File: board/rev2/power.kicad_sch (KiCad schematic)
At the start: 16 parts, among them J1 USB_C_Receptacle_USB2.0_14P, J2 Screw_Terminal_01x02, SW4 MS-22D28-G020, U7 TPD6S300A, U8 TPS62933F

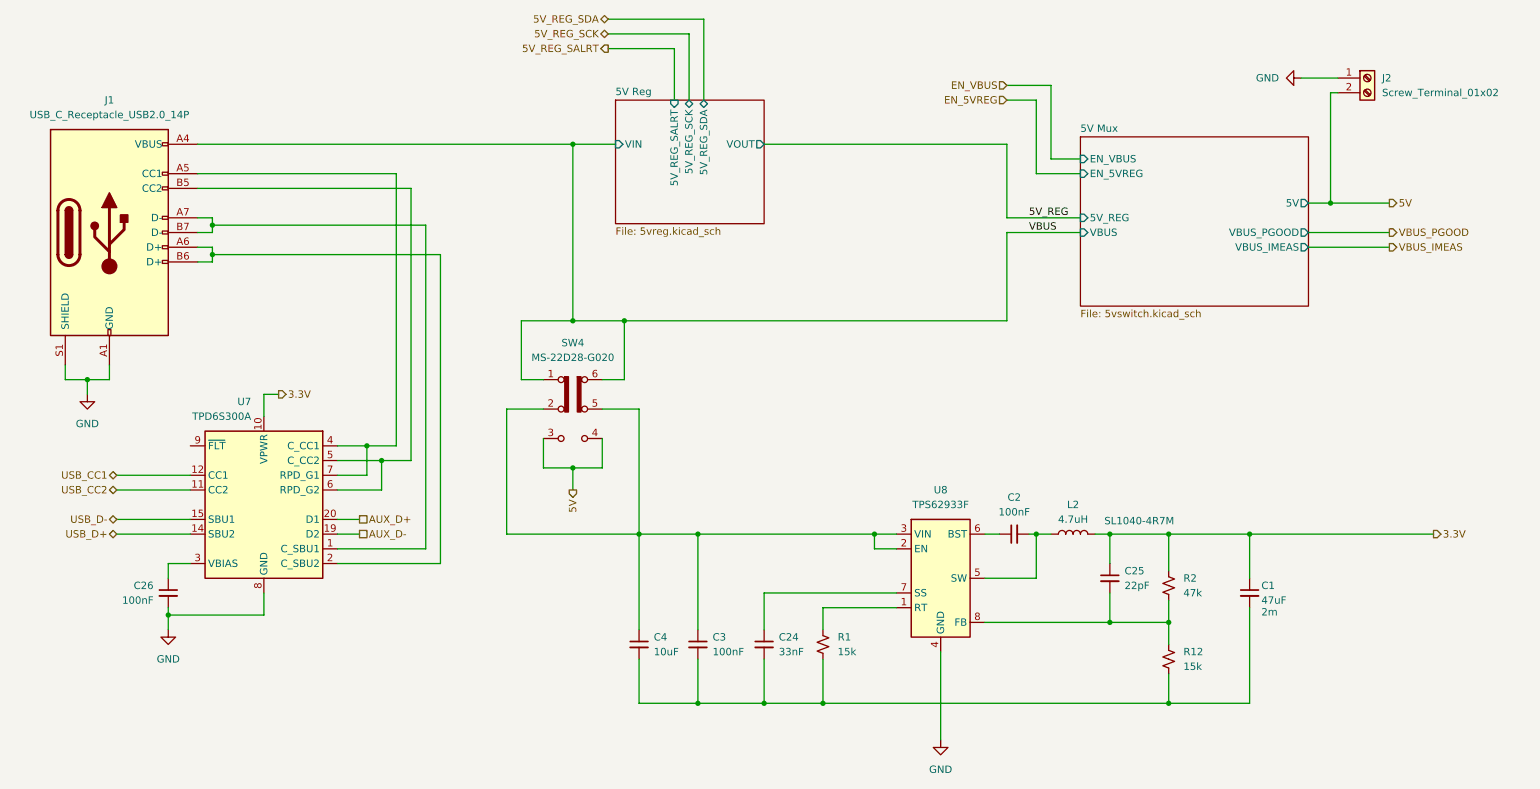
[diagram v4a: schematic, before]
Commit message: Start new PCB
- all footprints setup
- need to setup netclasses next, tho
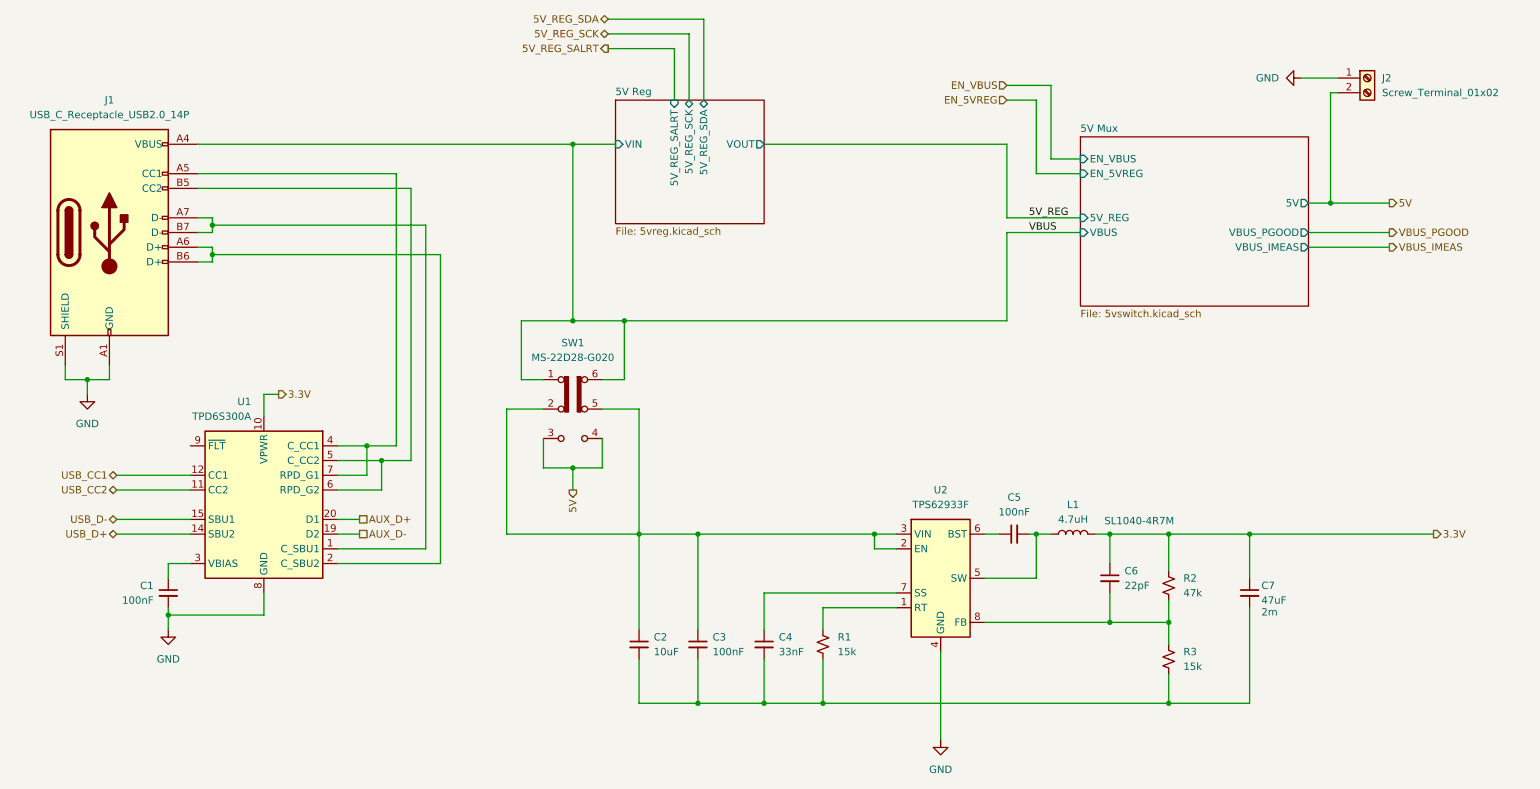
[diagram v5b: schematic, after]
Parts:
- J1: footprint (none) -> Connector_USB:USB_C_Receptacle_HRO_TYPE-C-31-M-12; Part (none) -> TYPE-C-31-M-12
- SW1: renamed from SW4; footprint (none) -> Switch_Slide_SMD:SW-SMD_MS-22D28-G020; Part (none) -> MS-22D28-G020
- U1: renamed from U7; Part (none) -> TPD6S300A
- U2: renamed from U8; Part (none) -> TPS62933F
- renumbered C26 to C1, C4 to C2, C24 to C4, C2 to C5, C25 to C6, C1 to C7, L2 to L1, R12 to R3
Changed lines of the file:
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@@
 		(on_board yes)
 		(dnp no)
-		(property "Reference" "C1"
+		(property "Reference" "C7"
 			(at 238.252 127 0)
 			(effects
@@
 			(project "mainboard"
 				(path "/32eb05c7-b4a6-42f3-8fb3-43453631100f/802d77e5-f72d-443e-abfe-d20b44acef6c"
-					(reference "C1")
+					(reference "C7")
 					(unit 1)
 				)
@@
 		(dnp no)
 		(fields_autoplaced yes)
-		(property "Reference" "#PWR021"
+		(property "Reference" "#PWR04"
 			(at 49.53 140.97 0)
 			(effects
@@
 			(project "mainboard"
 				(path "/32eb05c7-b4a6-42f3-8fb3-43453631100f/802d77e5-f72d-443e-abfe-d20b44acef6c"
-					(reference "#PWR021")
+					(reference "#PWR04")
 					(unit 1)
 				)
@@
 		(dnp no)
 		(fields_autoplaced yes)
-		(property "Reference" "C2"
+		(property "Reference" "C5"
 			(at 195.5863 111.76 90)
 			(effects
@@
 			(project ""
 				(path "/32eb05c7-b4a6-42f3-8fb3-43453631100f/802d77e5-f72d-443e-abfe-d20b44acef6c"
-					(reference "C2")
+					(reference "C5")
 					(unit 1)
 				)
@@
 		(on_board yes)
 		(dnp no)
-		(property "Reference" "SW4"
+		(property "Reference" "SW1"
 			(at 119.38 85.09 0)
 			(effects
@@
 			)
 		)
-		(property "Footprint" ""
+		(property "Footprint" "Switch_Slide_SMD:SW-SMD_MS-22D28-G020"
 			(at 133.35 91.44 0)
 			(effects
@@
 			)
 		)
+		(property "Part" "MS-22D28-G020"
+			(at 119.38 96.52 0)
+			(effects
+				(font
+					(size 1.27 1.27)
+				)
+				(hide yes)
+			)
+		)
 		(pin "3"
 		)
@@
 			(project ""
 				(path "/32eb05c7-b4a6-42f3-8fb3-43453631100f/802d77e5-f72d-443e-abfe-d20b44acef6c"
-					(reference "SW4")
+					(reference "SW1")
 					(unit 1)
 				)
@@
 		(dnp no)
 		(fields_autoplaced yes)
-		(property "Reference" "R12"
+		(property "Reference" "R3"
 			(at 224.79 138.4299 0)
 			(effects
@@
 			(project "mainboard"
 				(path "/32eb05c7-b4a6-42f3-8fb3-43453631100f/802d77e5-f72d-443e-abfe-d20b44acef6c"
-					(reference "R12")
+					(reference "R3")
 					(unit 1)
 				)
@@
 		(dnp no)
 		(fields_autoplaced yes)
-		(property "Reference" "U8"
+		(property "Reference" "U2"
 			(at 182.88 110.49 0)
 			(effects
@@
 			)
 		)
+		(property "Part" "TPS62933F"
+			(at 182.88 125.73 0)
+			(effects
+				(font
+					(size 1.27 1.27)
+				)
+				(hide yes)
+			)
+		)
 		(pin "7"
 		)
@@
 			(project ""
 				(path "/32eb05c7-b4a6-42f3-8fb3-43453631100f/802d77e5-f72d-443e-abfe-d20b44acef6c"
-					(reference "U8")
+					(reference "U2")
 					(unit 1)
 				)
@@
 			)
 		)
-		(property "Footprint" ""
+		(property "Footprint" "Connector_USB:USB_C_Receptacle_HRO_TYPE-C-31-M-12"
 			(at 43.18 66.04 0)
 			(effects
@@
 					(size 1.27 1.27)
 					(color 255 255 194 1)
+				)
+				(hide yes)
+			)
+		)
+		(property "Part" "TYPE-C-31-M-12"
+			(at 39.37 66.04 0)
+			(effects
+				(font
+					(size 1.27 1.27)
 				)
 				(hide yes)
@@
 		(dnp no)
 		(fields_autoplaced yes)
-		(property "Reference" "C26"
+		(property "Reference" "C1"
 			(at 46.99 127.0062 0)
 			(effects
@@
 			(project "mainboard"
 				(path "/32eb05c7-b4a6-42f3-8fb3-43453631100f/802d77e5-f72d-443e-abfe-d20b44acef6c"
-					(reference "C26")
+					(reference "C1")
 					(unit 1)
 				)
@@
 		(dnp no)
 		(fields_autoplaced yes)
-		(property "Reference" "#PWR010"
+		(property "Reference" "#PWR06"
 			(at 238.76 39.37 0)
 			(effects
@@
 			(project "mainboard"
 				(path "/32eb05c7-b4a6-42f3-8fb3-43453631100f/802d77e5-f72d-443e-abfe-d20b44acef6c"
-					(reference "#PWR010")
+					(reference "#PWR06")
 					(unit 1)
 				)
@@
 		(dnp no)
 		(fields_autoplaced yes)
-		(property "Reference" "C25"
+		(property "Reference" "C6"
 			(at 214.63 124.4662 0)
 			(effects
@@
 			(project "mainboard"
 				(path "/32eb05c7-b4a6-42f3-8fb3-43453631100f/802d77e5-f72d-443e-abfe-d20b44acef6c"
-					(reference "C25")
+					(reference "C6")
 					(unit 1)
 				)
@@
 		(dnp no)
 		(fields_autoplaced yes)
-		(property "Reference" "C24"
+		(property "Reference" "C4"
 			(at 154.94 135.8962 0)
 			(effects
@@
 			(project "mainboard"
 				(path "/32eb05c7-b4a6-42f3-8fb3-43453631100f/802d77e5-f72d-443e-abfe-d20b44acef6c"
-					(reference "C24")
+					(reference "C4")
 					(unit 1)
 				)
@@
 		(dnp no)
 		(fields_autoplaced yes)
-		(property "Reference" "C4"
+		(property "Reference" "C2"
 			(at 133.35 135.8962 0)
 			(effects
@@
 			(project "mainboard"
 				(path "/32eb05c7-b4a6-42f3-8fb3-43453631100f/802d77e5-f72d-443e-abfe-d20b44acef6c"
-					(reference "C4")
+					(reference "C2")
 					(unit 1)
 				)
@@
 		(on_board yes)
 		(dnp no)
-		(property "Reference" "L2"
+		(property "Reference" "L1"
 			(at 205.74 113.03 90)
 			(effects
@@
 			(project ""
 				(path "/32eb05c7-b4a6-42f3-8fb3-43453631100f/802d77e5-f72d-443e-abfe-d20b44acef6c"
-					(reference "L2")
+					(reference "L1")
 					(unit 1)
 				)
@@
 		(dnp no)
 		(fields_autoplaced yes)
-		(property "Reference" "#PWR07"
+		(property "Reference" "#PWR03"
 			(at 35.56 100.33 0)
 			(effects
@@
 			(project "mainboard"
 				(path "/32eb05c7-b4a6-42f3-8fb3-43453631100f/802d77e5-f72d-443e-abfe-d20b44acef6c"
-					(reference "#PWR07")
+					(reference "#PWR03")
 					(unit 1)
 				)
@@
 		(dnp no)
 		(fields_autoplaced yes)
-		(property "Reference" "#PWR04"
+		(property "Reference" "#PWR05"
 			(at 182.88 160.02 0)
 			(effects
@@
 			(project "mainboard"
 				(path "/32eb05c7-b4a6-42f3-8fb3-43453631100f/802d77e5-f72d-443e-abfe-d20b44acef6c"
-					(reference "#PWR04")
+					(reference "#PWR05")
 					(unit 1)
 				)
@@
 		(dnp no)
 		(fields_autoplaced yes)
-		(property "Reference" "U7"
+		(property "Reference" "U1"
 			(at 63.8459 95.25 0)
 			(effects
@@
 			)
 		)
+		(property "Part" "TPD6S300A"
+			(at 66.04 113.03 0)
+			(effects
+				(font
+					(size 1.27 1.27)
+				)
+				(hide yes)
+			)
+		)
 		(pin "1"
 		)
@@
 			(project "mainboard"
 				(path "/32eb05c7-b4a6-42f3-8fb3-43453631100f/802d77e5-f72d-443e-abfe-d20b44acef6c"
-					(reference "U7")
-					(unit 1)
-				)
+					(reference "U1")
+					(unit 1)
+				)

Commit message: Add netclasses, more footprints, fix ERC
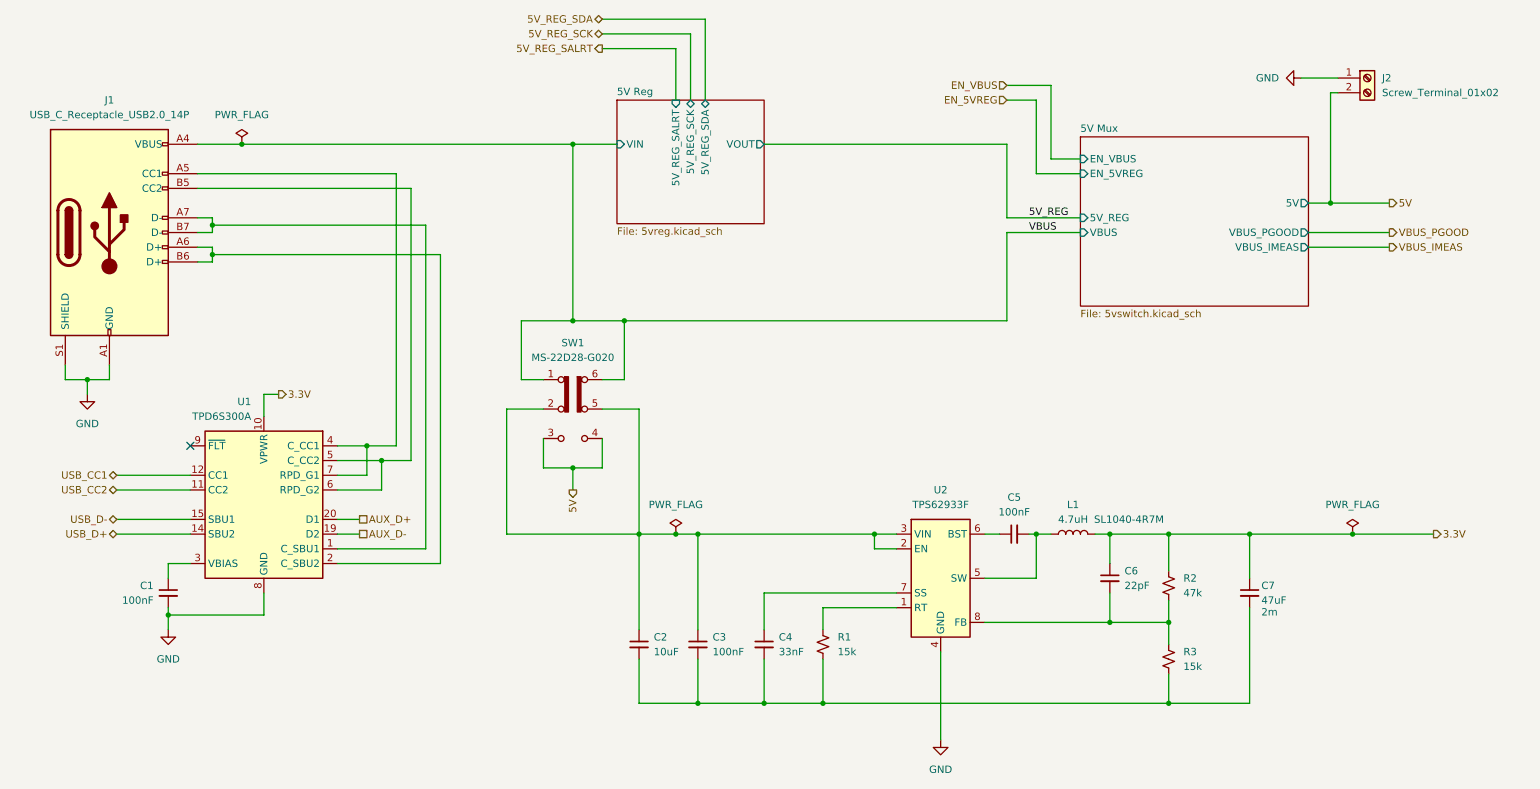
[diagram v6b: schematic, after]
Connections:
- no-connect marks 0 -> 1

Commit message: Really finish rev2 board schematic
- fix some more footprints
  - move to real SD card holder, for example
- repair part numbers
- add LCSC part refs to everything
- add even more caps to the 3.3V reg output
  - really should use an LDO but meh it should be fine

total BOM cost for 5 of them is apparently 160 CAD, or like 32 dollars
each (don't think that includes the feeder fees tho)
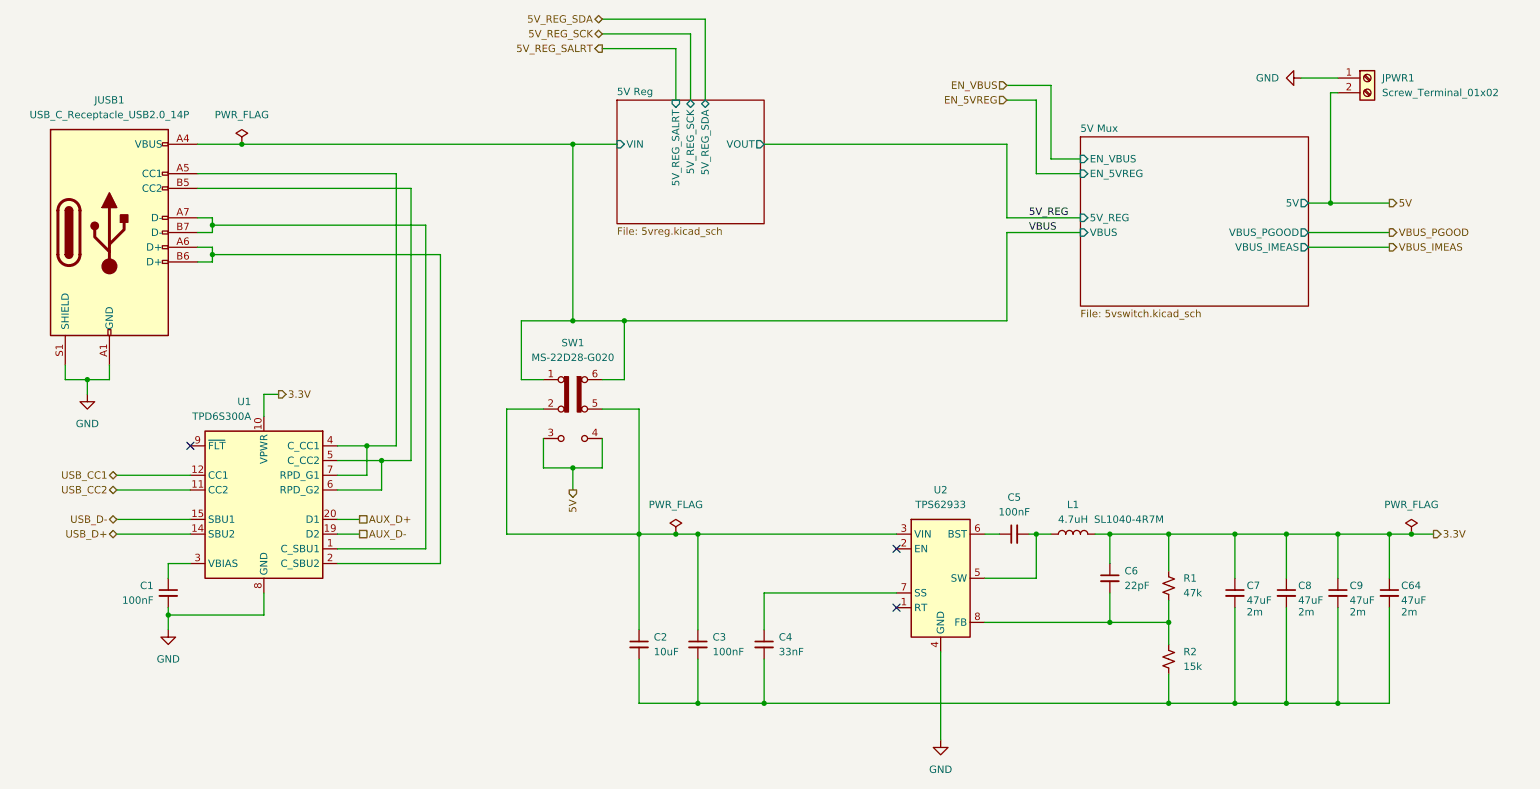
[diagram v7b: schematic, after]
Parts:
- removed R1: 15k, Resistor_SMD:R_0805_2012Metric, symbol Device:R_Small_US
- added C64, C8, C9: 47uF, Capacitor_SMD:C_1206_3216Metric, symbol Device:C_Small
- C1, C3, C5: LCSC (none) -> C307331
- C2: LCSC (none) -> C13585
- C4: LCSC (none) -> C21117
- C6: footprint Capacitor_SMD:C_0402_1005Metric -> Capacitor_SMD:C_0603_1608Metric; LCSC (none) -> C1653; Part 0402CG220J500NT -> CL10C220JB8NNNC
- C7: LCSC (none) -> C96123
- JUSB1: renamed from J1; LCSC (none) -> C165948
- L1: LCSC (none) -> C22463838
- R1: renamed from R2; LCSC (none) -> C17713
- R2: renamed from R3; LCSC (none) -> C17475
- SW1: LCSC (none) -> C963205
- U1: LCSC (none) -> C2876380; Part TPD6S300A -> TPD6S300ARUKR
- U2: value TPS62933F -> TPS62933; LCSC (none) -> C3200405; Part TPS62933F -> TPS62933DRLR
- renumbered J2 to JPWR1
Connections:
- net 3.3V: now also C64.1, C8.1, C9.1
- net at C2.2, C3.2, C4.2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: now also C64.2, C8.2, C9.2
- net at C2.1, C3.1, SW1.2 (B)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: no longer U2.2 (EN)
- no-connect marks 1 -> 3
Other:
- moved on the sheet: C7

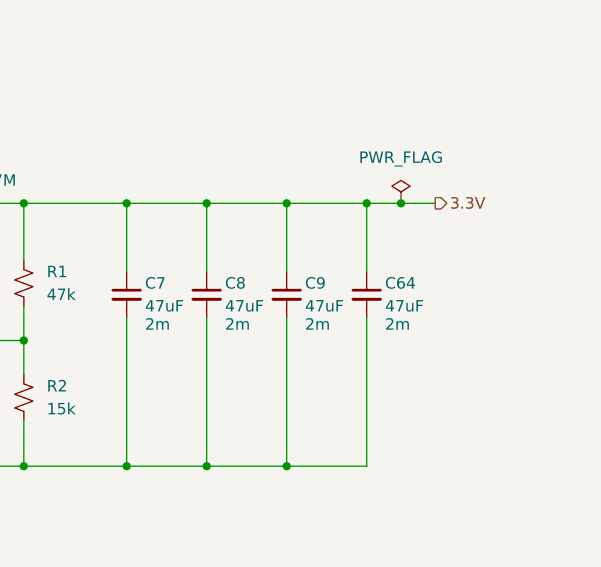
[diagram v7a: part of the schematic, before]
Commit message: Start board
add a few extra bypass caps too, and swap some pins on the USB mux

i forgot to add a bypass cap on the tpd6s so that also needs to happen

truly 63 capacitors is not enough
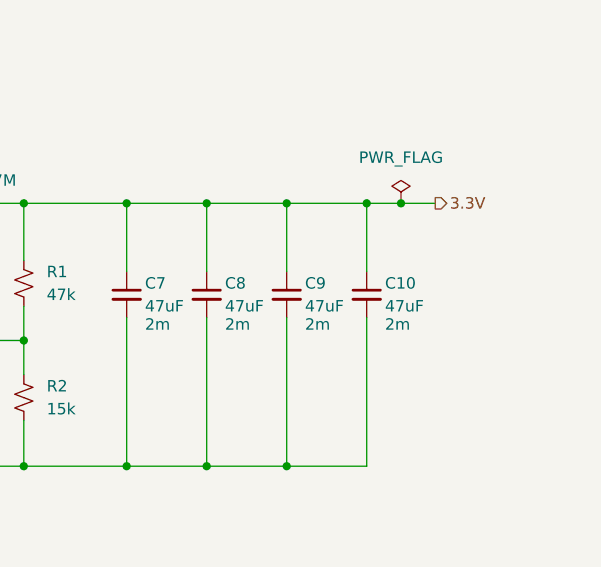
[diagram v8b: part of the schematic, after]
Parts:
- renumbered C64 to C10
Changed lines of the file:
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@@
 		(on_board yes)
 		(dnp no)
-		(property "Reference" "C64"
+		(property "Reference" "C10"
 			(at 262.382 127 0)
 			(effects
@@
 			(project "mainboard"
 				(path "/32eb05c7-b4a6-42f3-8fb3-43453631100f/802d77e5-f72d-443e-abfe-d20b44acef6c"
-					(reference "C64")
+					(reference "C10")
 					(unit 1)
 				)
